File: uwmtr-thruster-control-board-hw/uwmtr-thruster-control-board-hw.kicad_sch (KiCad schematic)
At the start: 2 parts, among them J1 Conn_01x13_Pin, U1 TI_MCF8316A

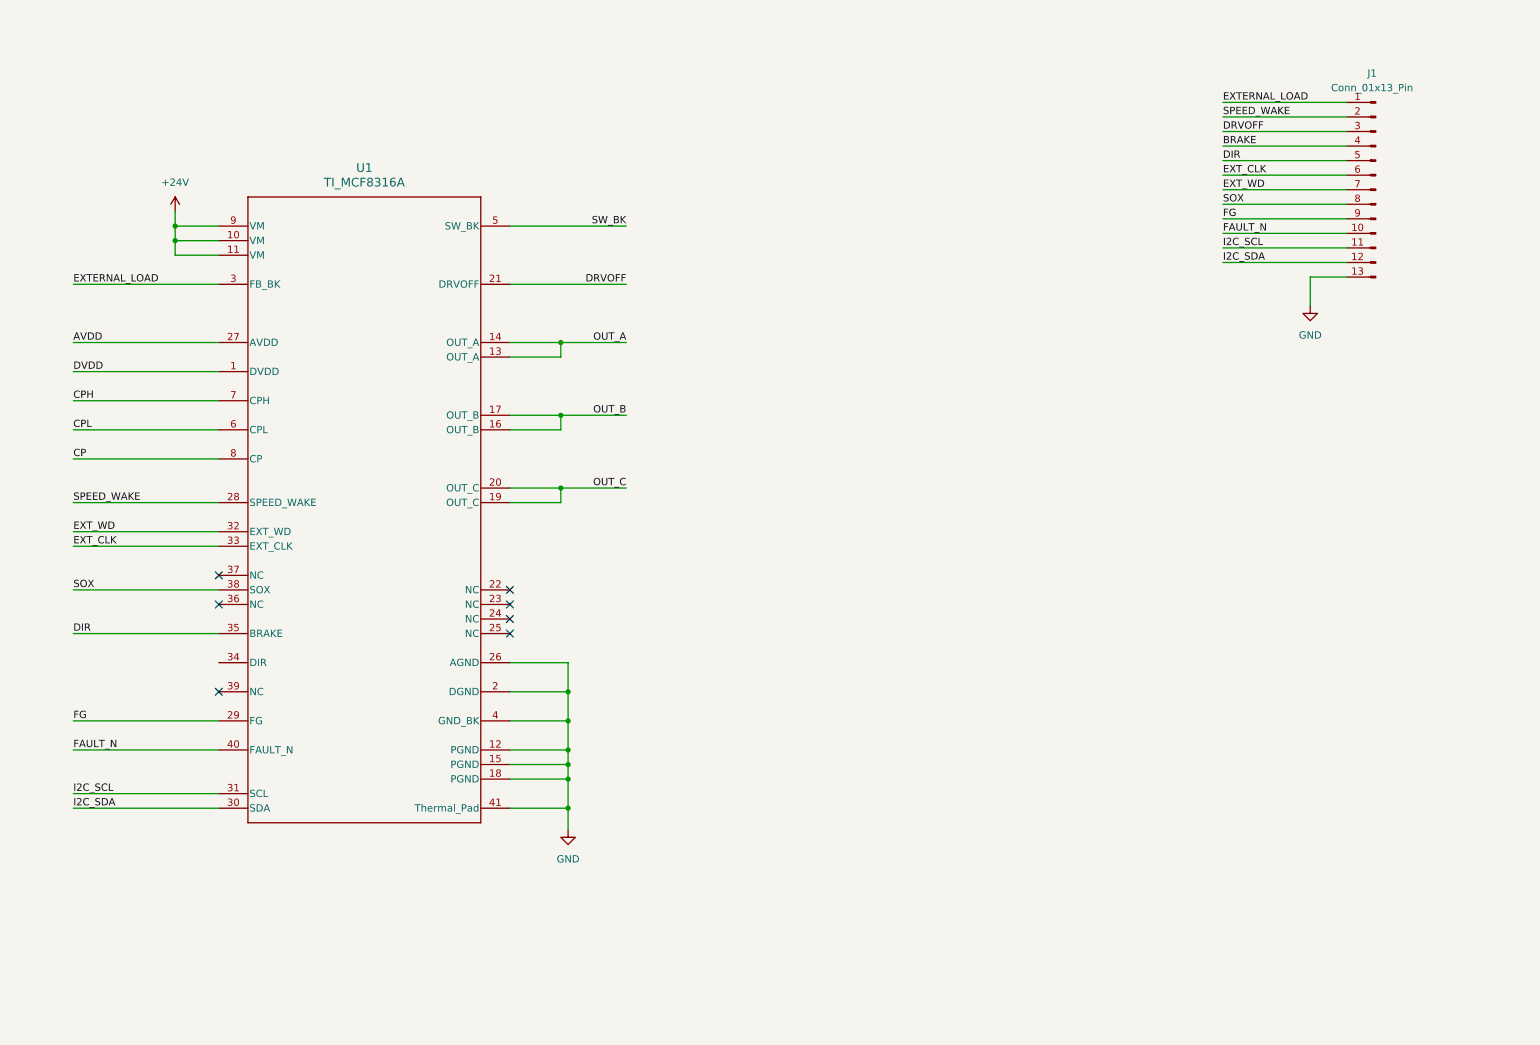
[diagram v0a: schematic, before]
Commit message: Fixing git tree and commiting new schematic revision.
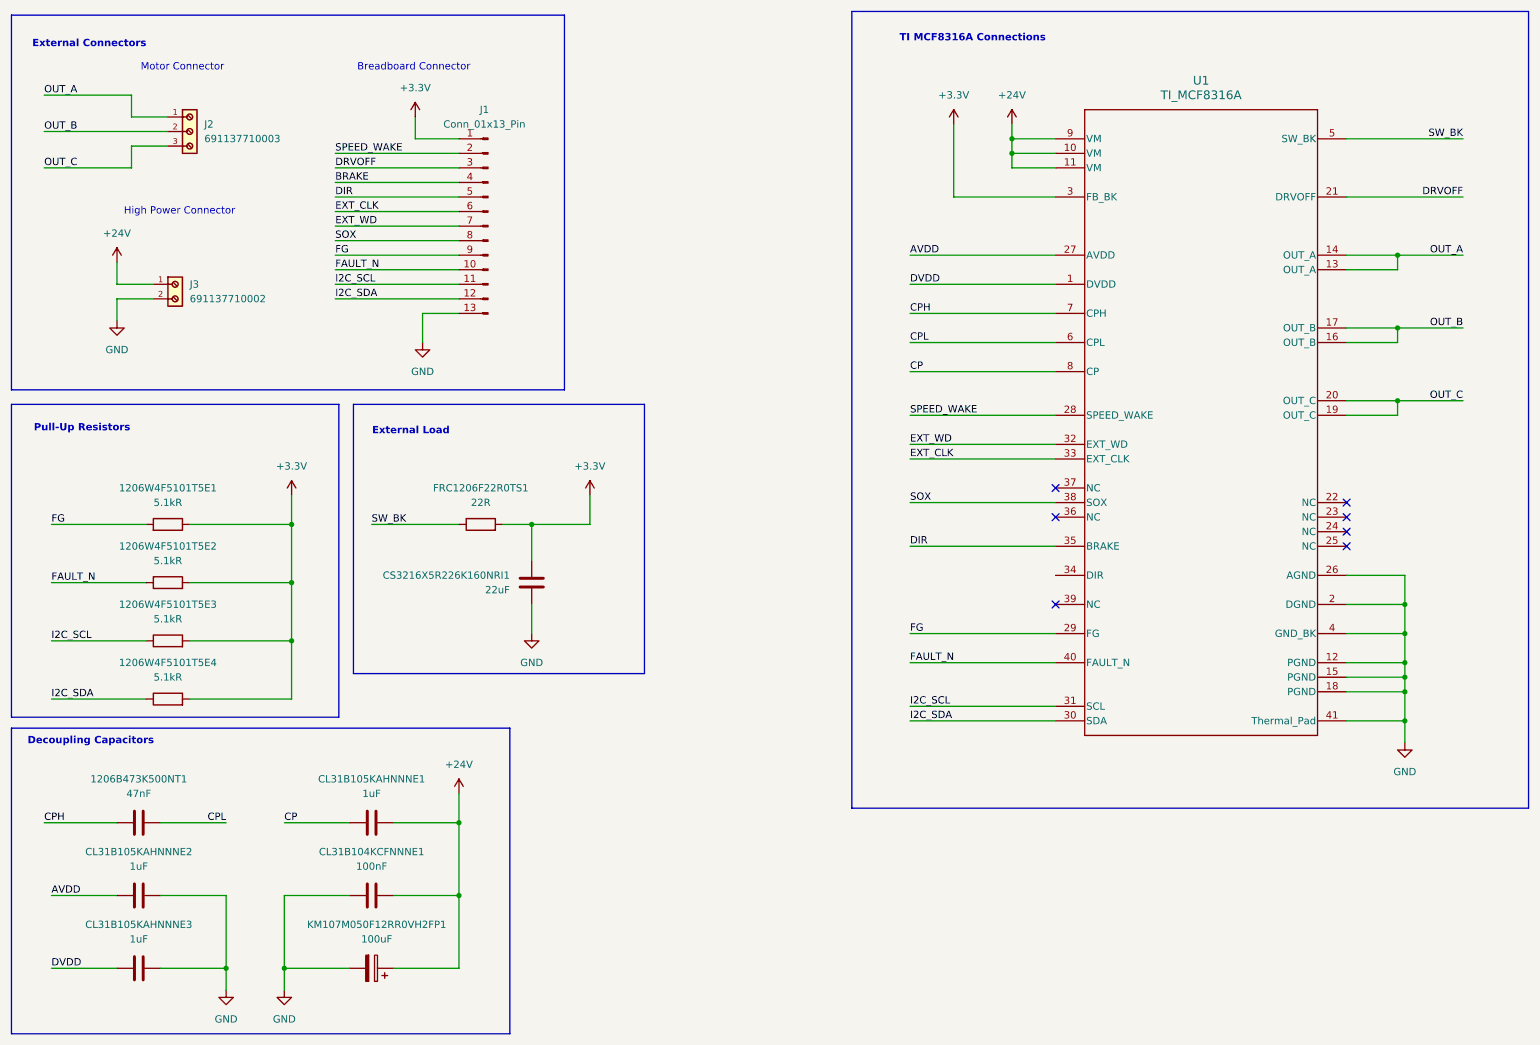
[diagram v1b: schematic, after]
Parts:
- added 1206B473K500NT1: 47nF, Capacitor_SMD:C_1206_3216Metric, symbol uwmtr-thruster-control-board-hw-custom-symbols:1206B473K500NT
- added 1206W4F5101T5E1, 1206W4F5101T5E2, 1206W4F5101T5E3, 1206W4F5101T5E4: 5.1kR, Resistor_SMD:R_1206_3216Metric, symbol uwmtr-thruster-control-board-hw-custom-symbols:1206W4F5101T5E
- added CL31B104KCFNNNE1: 100nF, Capacitor_SMD:C_1206_3216Metric, symbol uwmtr-thruster-control-board-hw-custom-symbols:CL31B104KCFNNNE
- added CL31B105KAHNNNE1, CL31B105KAHNNNE2, CL31B105KAHNNNE3: 1uF, Capacitor_SMD:C_1206_3216Metric, symbol uwmtr-thruster-control-board-hw-custom-symbols:CL31B105KAHNNNE
- added CS3216X5R226K160NRI1: 22uF, Capacitor_SMD:C_1206_3216Metric, symbol uwmtr-thruster-control-board-hw-custom-symbols:CS3216X5R226K160NRI
- added FRC1206F22R0TS1: 22R, Resistor_SMD:R_1206_3216Metric, symbol uwmtr-thruster-control-board-hw-custom-symbols:FRC1206F22R0TS
- added J2: 691137710003, 691137710003:691137710003, symbol uwmtr-thruster-control-board-hw-custom-symbols:691137710003
- added J3: 691137710002, uwmtr-thruster-control-board-hw-footprints:691137710002, symbol uwmtr-thruster-control-board-hw-custom-symbols:691137710002
- added KM107M050F12RR0VH2FP1: 100uF, Capacitor_THT:C_Radial_D8.0mm_H11.5mm_P3.50mm, symbol uwmtr-thruster-control-board-hw-custom-symbols:KM107M050F12RR0VH2FP0
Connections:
- net +24V: now also CL31B104KCFNNNE1.2, CL31B105KAHNNNE1.1, J3.1, KM107M050F12RR0VH2FP1.1
- net AVDD: now also CL31B105KAHNNNE2.2
- net CP: now also CL31B105KAHNNNE1.2
- net CPH: now also 1206B473K500NT1.1
- net CPL: now also 1206B473K500NT1.2
- net DVDD: now also CL31B105KAHNNNE3.2
- net FAULT_N: now also 1206W4F5101T5E2.1
- net FG: now also 1206W4F5101T5E1.2
- net GND: now also CL31B104KCFNNNE1.1, CL31B105KAHNNNE2.1, CL31B105KAHNNNE3.1, CS3216X5R226K160NRI1.2, J3.2, KM107M050F12RR0VH2FP1.2
- net I2C_SCL: now also 1206W4F5101T5E3.1
- net I2C_SDA: now also 1206W4F5101T5E4.1
- net OUT_A: now also J2.1
- net OUT_B: now also J2.2
- net OUT_C: now also J2.3
- net SW_BK: now also FRC1206F22R0TS1.1
- net EXTERNAL_LOAD renamed +3.3V
- net +3.3V: now also 1206W4F5101T5E1.1, 1206W4F5101T5E2.2, 1206W4F5101T5E3.2, 1206W4F5101T5E4.2, CS3216X5R226K160NRI1.1, FRC1206F22R0TS1.2
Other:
- note added: "Breadboard Connector"
- note added: "Decoupling Capacitors"
- note added: "External Connectors"
- note added: "External Load"
- note added: "High Power Connector"
- note added: "Motor Connector"
- note added: "Pull-Up Resistors"
- note added: "TI MCF8316A Connections"
- moved on the sheet: J1, U1

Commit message: Adding a bit of routing
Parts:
- J2: footprint 691137710003:691137710003 -> uwmtr-thruster-control-board-hw-footprints:691137710003
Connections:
- net BRAKE: now also U1.35 (BRAKE)
- net DIR: now also U1.34 (DIR); no longer U1.35 (BRAKE)
- net FAULT_N: now also J1.12 (Pin_12); no longer J1.10 (Pin_10)
- net GND: now also J1.2 (Pin_2); no longer J1.13 (Pin_13)
- net I2C_SDA: now also J1.10 (Pin_10); no longer J1.12 (Pin_12)
- net SPEED_WAKE: now also J1.13 (Pin_13); no longer J1.2 (Pin_2)
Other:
- note added: "Power Flags"

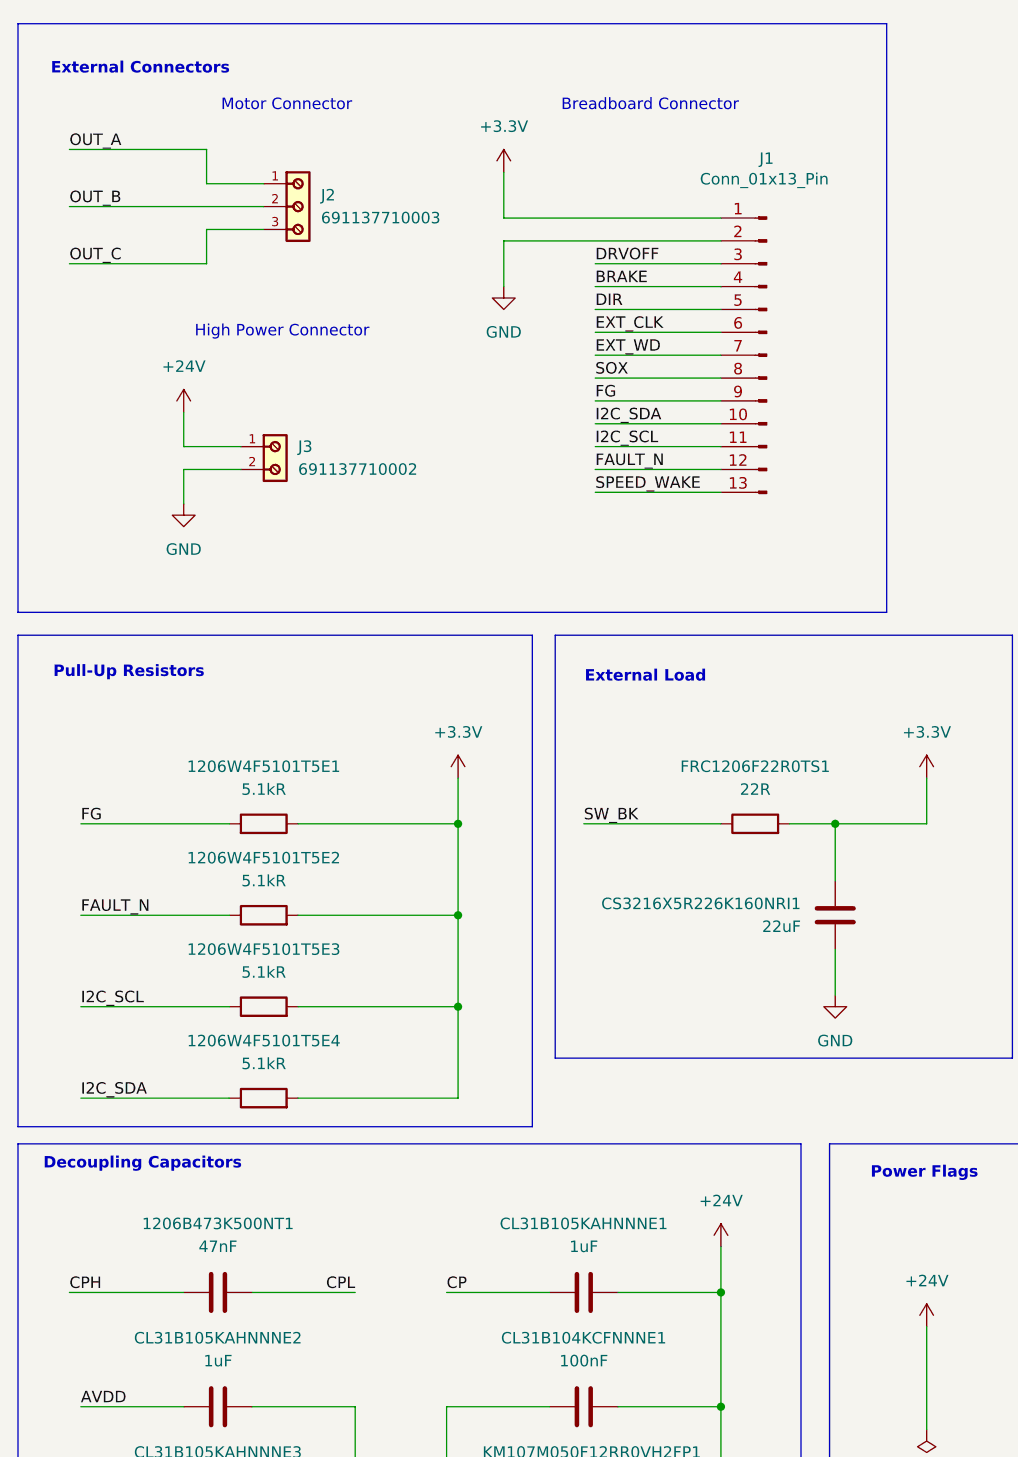
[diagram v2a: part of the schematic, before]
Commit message: Completing component placement for layout and replacing the resistor
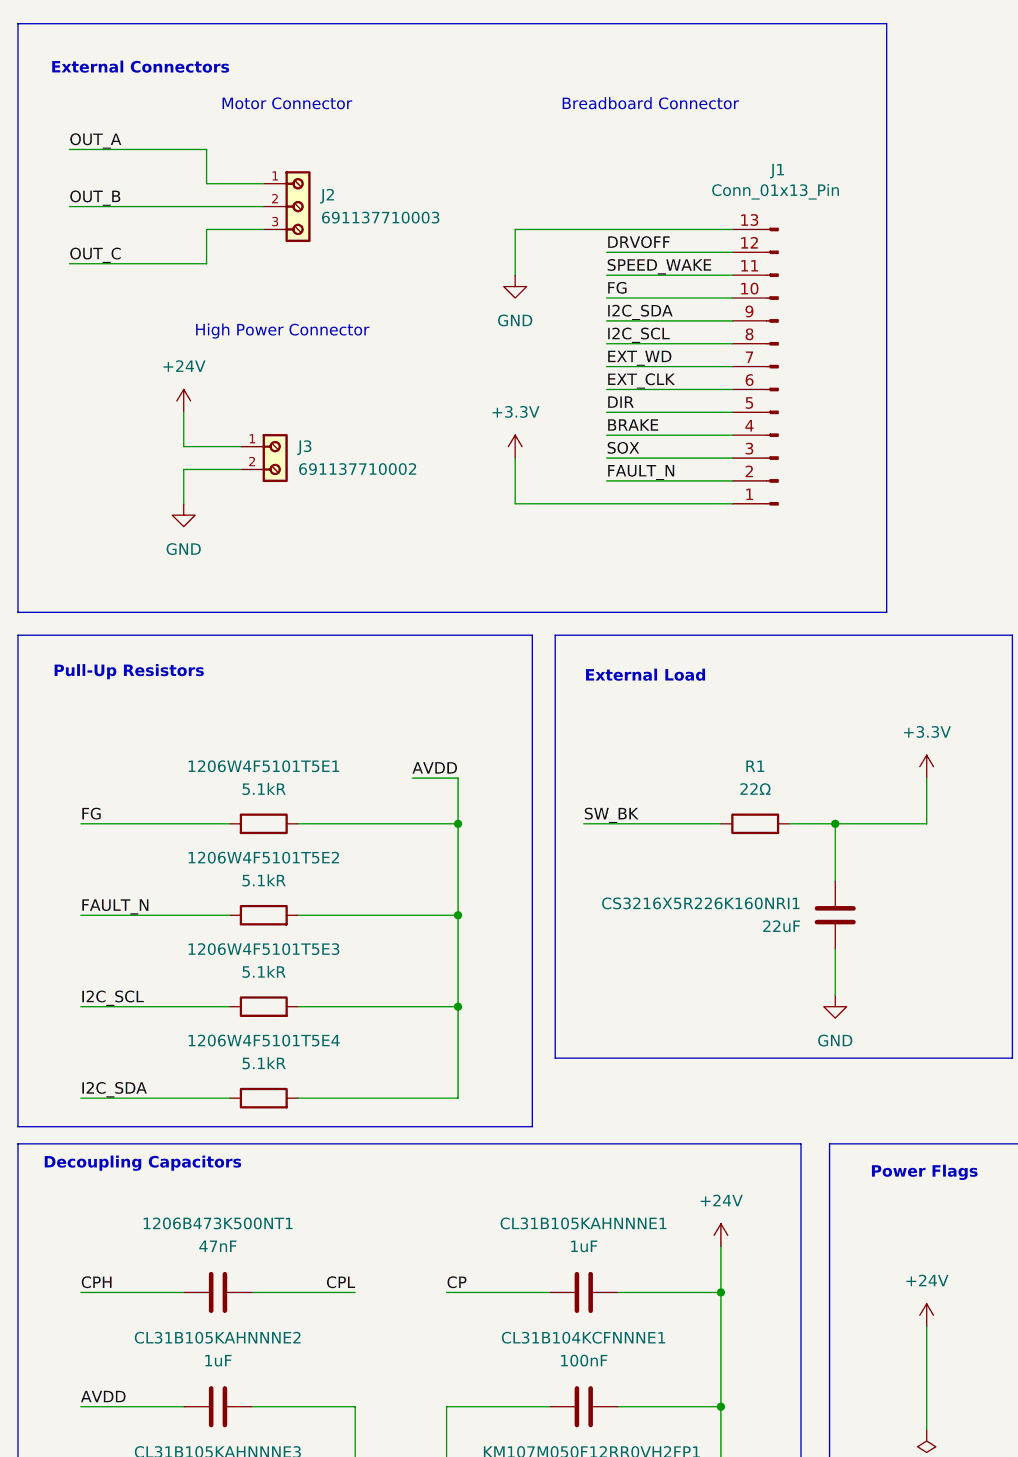
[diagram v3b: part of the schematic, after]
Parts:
- removed FRC1206F22R0TS1: 22R, Resistor_SMD:R_1206_3216Metric, symbol uwmtr-thruster-control-board-hw-custom-symbols:FRC1206F22R0TS
- added R1: 22Ω, Resistor_THT:R_Axial_DIN0207_L6.3mm_D2.5mm_P10.16mm_Horizontal, symbol Device:R
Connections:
- net +3.3V: now also R1.2; no longer 1206W4F5101T5E1.1, 1206W4F5101T5E2.2, 1206W4F5101T5E3.2, 1206W4F5101T5E4.2
- net AVDD: now also 1206W4F5101T5E1.1, 1206W4F5101T5E2.2, 1206W4F5101T5E3.2, 1206W4F5101T5E4.2
- net DRVOFF: now also J1.12 (Pin_2); no longer J1.3 (Pin_3)
- net FAULT_N: now also J1.2 (Pin_12); no longer J1.12 (Pin_12)
- net FG: now also J1.10 (Pin_4); no longer J1.9 (Pin_9)
- net GND: now also J1.13 (Pin_1); no longer J1.2 (Pin_2)
- net I2C_SCL: now also J1.8 (Pin_6); no longer J1.11 (Pin_11)
- net I2C_SDA: now also J1.9 (Pin_5); no longer J1.10 (Pin_10)
- net SOX: now also J1.3 (Pin_11); no longer J1.8 (Pin_8)
- net SPEED_WAKE: now also J1.11 (Pin_3); no longer J1.13 (Pin_13)
- net SW_BK: now also R1.1

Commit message: Completing layout
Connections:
- net GND renamed AGND
- net AGND: no longer CL31B104KCFNNNE1.1, J3.2, KM107M050F12RR0VH2FP1.2, U1.12 (PGND), U1.15 (PGND), U1.18 (PGND)
- new net PGND: CL31B104KCFNNNE1.1, J3.2, KM107M050F12RR0VH2FP1.2, U1.12 (PGND), U1.15 (PGND), U1.18 (PGND)
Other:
- note added: "External Load (+3.3V)"
- note removed: "External Load"
- moved on the sheet: 1206W4F5101T5E1, 1206W4F5101T5E2, 1206W4F5101T5E3, 1206W4F5101T5E4, CS3216X5R226K160NRI1, J1, J2, J3, R1, U1

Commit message: Creating all manufacturing files
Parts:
- U1: JLCPCB Part # (none) -> C3681167; LCSC C3681167 -> (none)
